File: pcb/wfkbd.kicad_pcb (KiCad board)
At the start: 2 copper layers, 132 x 98.5 mm, 106 parts, among them SW1 KEY, SW10 KEY, SW11 KEY, SW12 KEY, SW13 KEY, SW14 KEY, SW15 KEY, SW16 KEY, SW17 KEY, SW18 KEY, SW19 KEY, SW2 KEY, SW20 KEY, SW21 KEY, SW22 KEY, SW23 KEY, SW24 KEY, SW25 KEY, SW26 KEY, SW27 KEY, SW28 KEY, SW29 KEY, SW3 KEY, SW30 KEY, SW31 KEY, SW32 KEY, SW33 KEY, SW34 KEY, SW35 KEY, SW4 KEY, SW5 KEY, SW6 KEY, SW7 KEY, SW8 KEY, SW9 KEY, U1 ProMicro

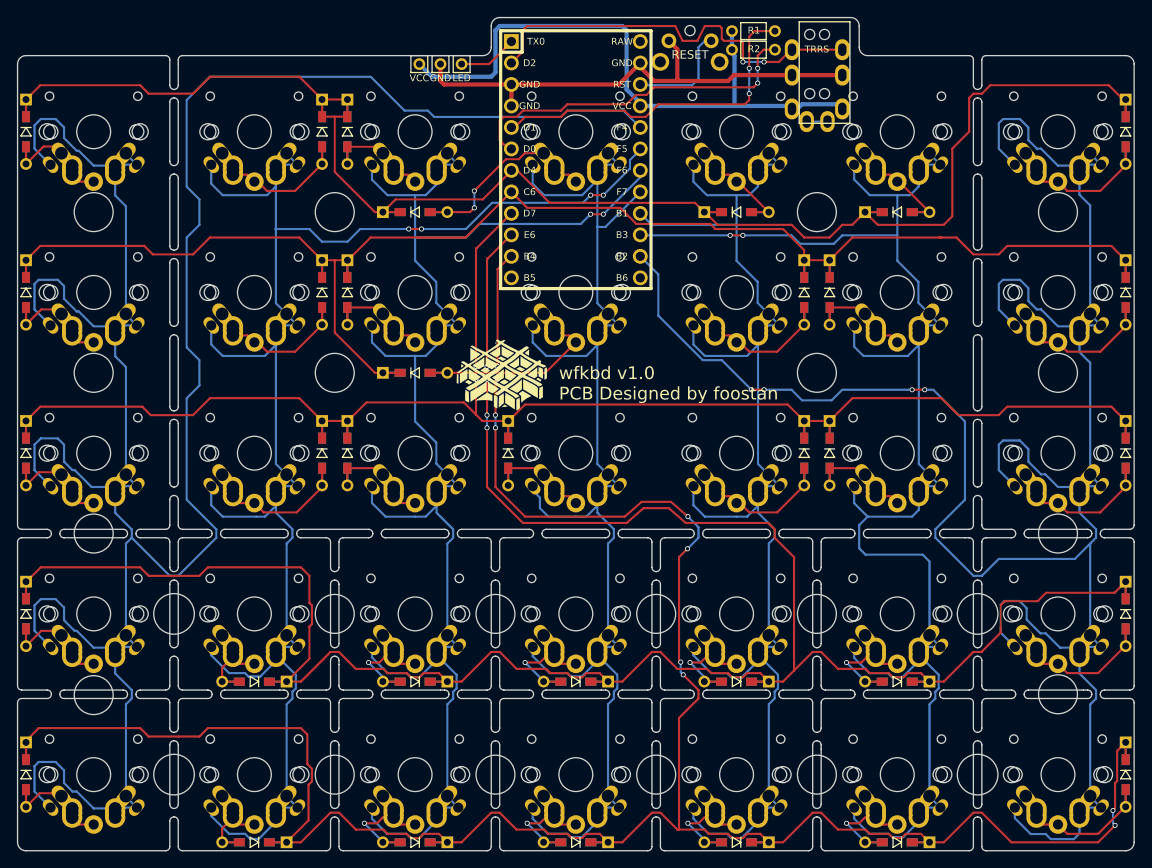
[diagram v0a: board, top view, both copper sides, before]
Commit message: Add GND filled zones (front & back)
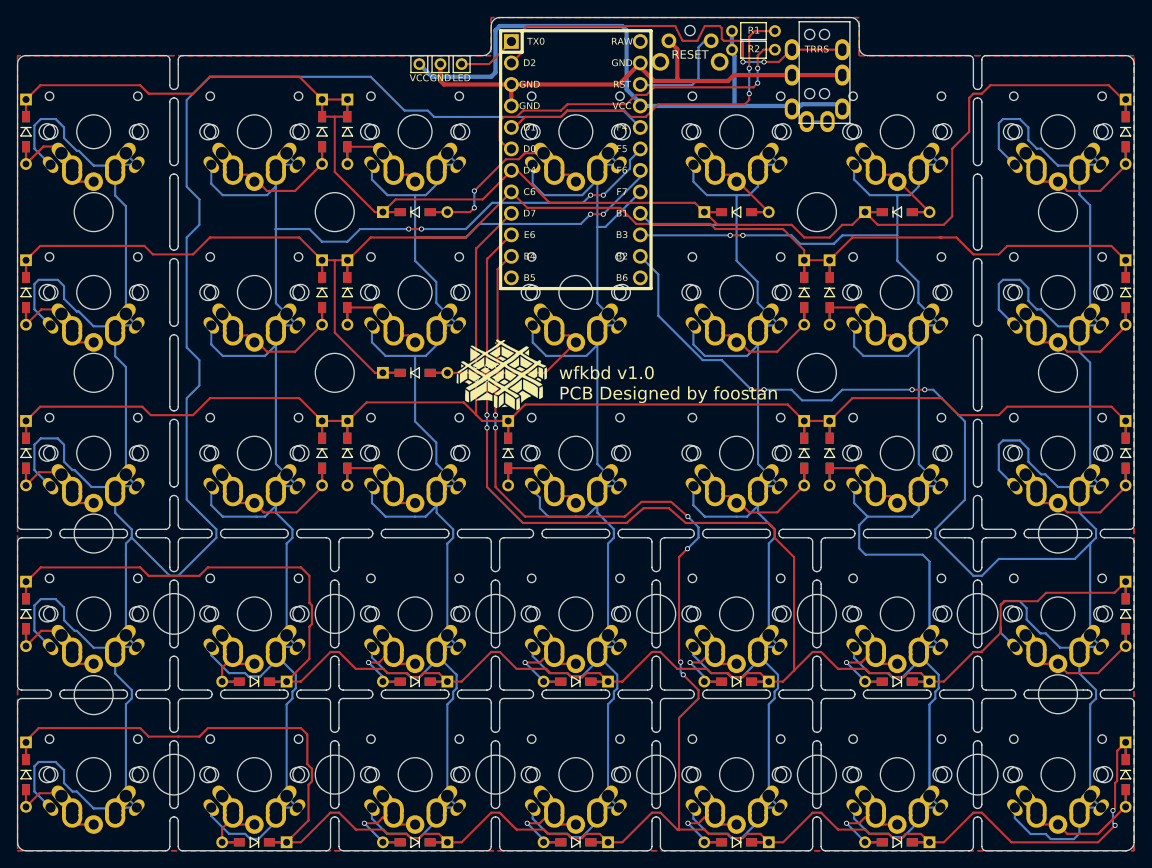
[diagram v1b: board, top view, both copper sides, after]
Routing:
- added copper zone on F.Cu, net (none)

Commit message: Add fill zone to back
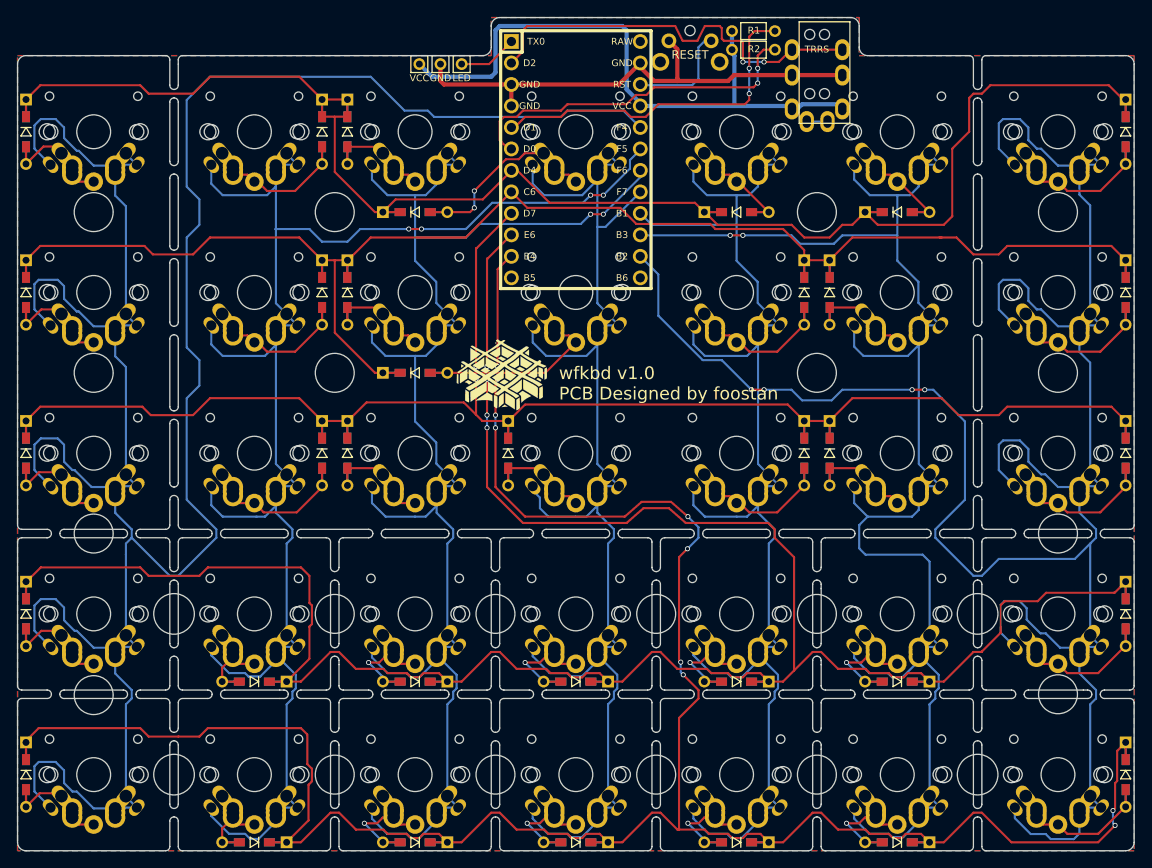
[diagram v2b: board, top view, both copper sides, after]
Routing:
- added copper zone on B.Cu, net (none)
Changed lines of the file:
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@@
-(kicad_pcb (version 20171130) (host pcbnew "(5.1.0-rc1-8-gc568fadec)")
+(kicad_pcb (version 20171130) (host pcbnew "(5.1.2-1)-1")
   (general
     (thickness 1.6)
@@
     (polygon
       (pts
-        (xy 41 41) (xy 41 135) (xy 173 135) (xy 173 41) (xy 140.5 41)
-        (xy 140.5 36.5) (xy 97 36.5) (xy 97 41)
+        (xy 140.5 41) (xy 173 41) (xy 173 135) (xy 41 135) (xy 41 41)
+        (xy 97 41) (xy 97 36.5) (xy 140.5 36.5)
       )
     )
   )
-  (zone (net 0) (net_name "") (layer F.Cu) (hatch edge 0.508)
+  (zone (net 0) (net_name "") (layer B.Cu) (hatch edge 0.508)
     (connect_pads (clearance 0.508))
     (min_thickness 0.254)
@@
     (polygon
       (pts
-        (xy 41 41) (xy 41 135) (xy 173 135) (xy 173 41) (xy 140.5 41)
-        (xy 140.5 36.5) (xy 97 36.5) (xy 97 41)
+        (xy 140.5 41) (xy 173 41) (xy 173 135) (xy 41 135) (xy 41 41)
+        (xy 97 41) (xy 97 36.5) (xy 140.5 36.5)
       )
     )
